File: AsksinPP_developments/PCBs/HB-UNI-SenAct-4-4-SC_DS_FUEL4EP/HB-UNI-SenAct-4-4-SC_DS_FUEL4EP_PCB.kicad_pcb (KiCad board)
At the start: 2 copper layers, 86 x 63 mm, 49 parts, among them J1 5V supply, J10 charge, J2 4x Push Buttons, J3 4x Relais, J4 5x LEDs, J5 ISP Programmer, J6 Accumulator, Q1 IRLU024N, Q2 BD238, Q4 IRF9Z34N, Q5 MCP1702-2802E_TO, SW1 SW_Push

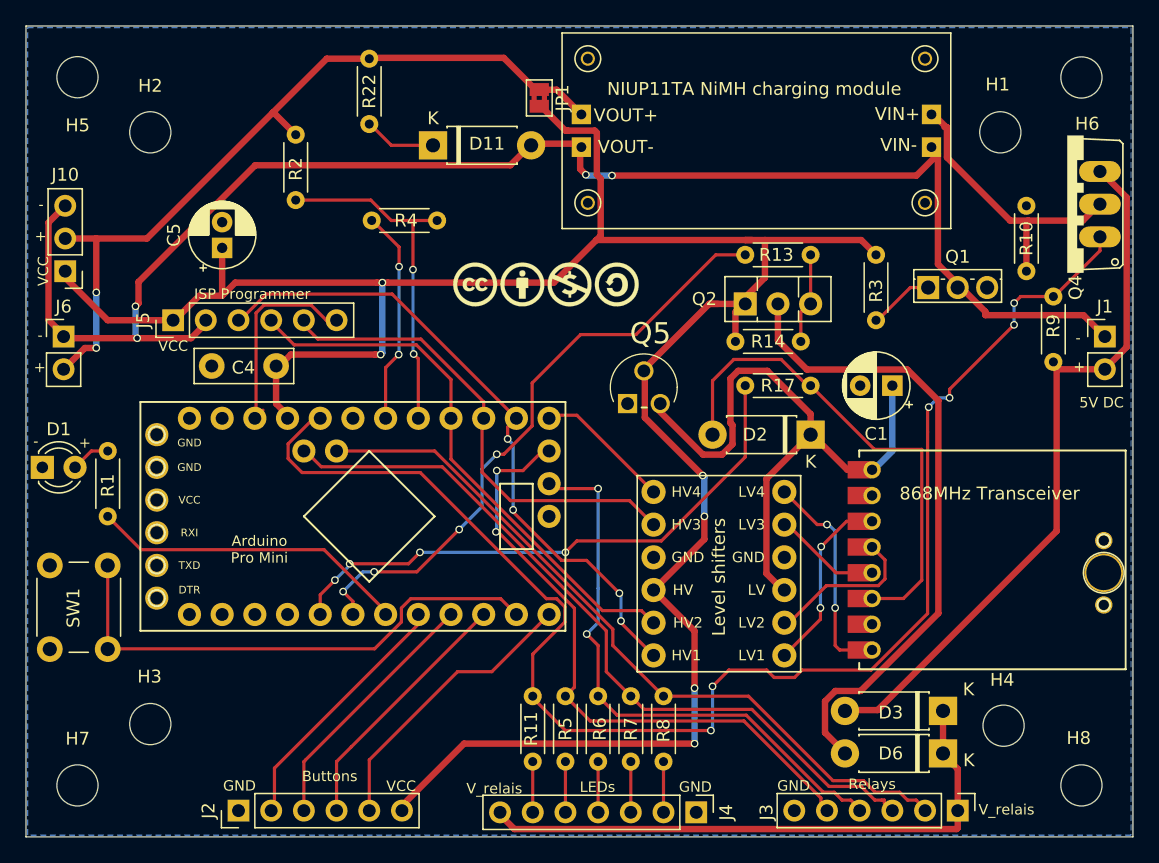
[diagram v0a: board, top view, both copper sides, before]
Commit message: PCBs/HB-UNI-SenAct-4-4-SC_DS_FUEL4EP: small fixes; HB-UNI-Sensor1-THPD-SHT85: Small flaw detected: SYSCLK calibration is missing; Please wait a bit for a fix
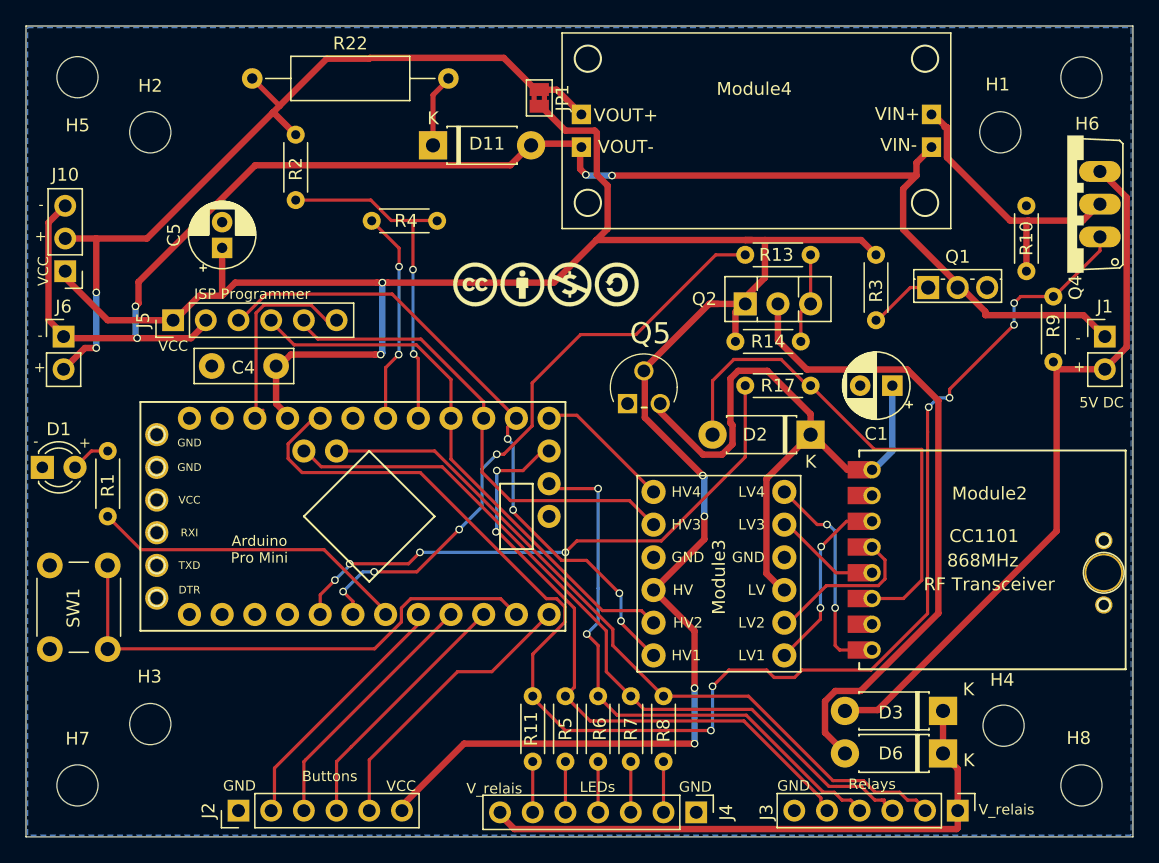
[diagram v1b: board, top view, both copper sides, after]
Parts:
- Module2: renamed from 868MHz Transceiver
- Module3: renamed from Level shifters; value Level Shifters -> 4_channel_LOGIC_LEVEL_CONVERTER
- Module4: renamed from NIUP11TA NiMH charging module
- R22: footprint Resistor_THT:R_Axial_DIN0204_L3.6mm_D1.6mm_P5.08mm_Horizontal -> Resistor_THT:R_Axial_DIN0309_L9.0mm_D3.2mm_P15.24mm_Horizontal
- moved R22 9.22 mm to (17.6, 4.08), turned to 0 degrees
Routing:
- net /plusBAT: track 62.3 -> 65.3 mm

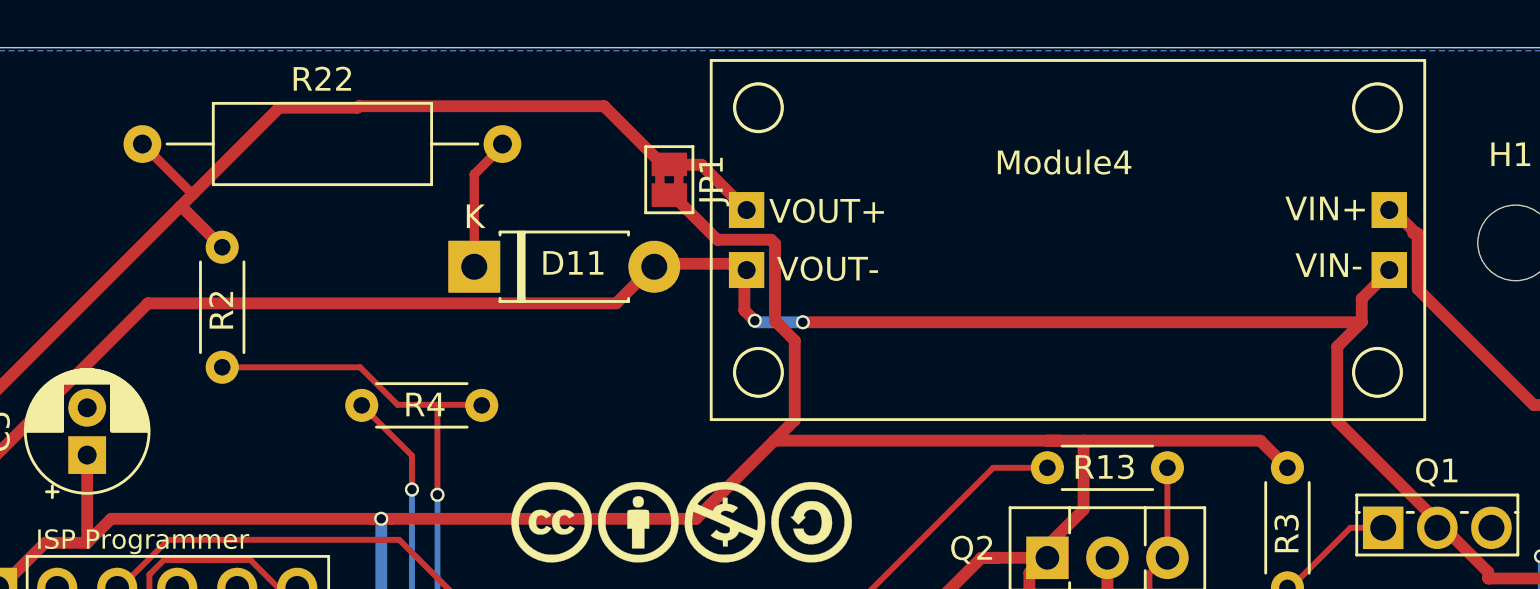
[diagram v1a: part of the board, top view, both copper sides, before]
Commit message: PCBs/HB-UNI-SenAct-4-4-SC_DS_FUEL4EP and PCBs/HM-LC-Bl1-FM_FUEL4EP: fixes of some geometry flaws that popped up during trial assembly
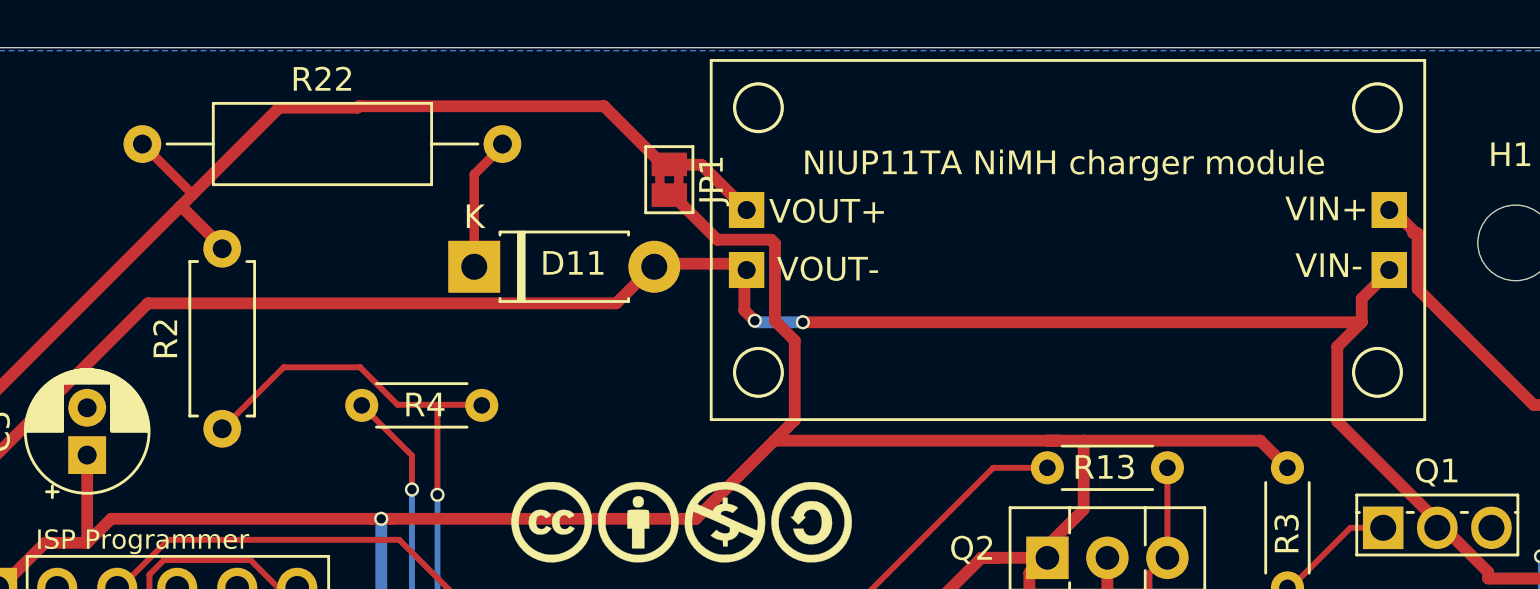
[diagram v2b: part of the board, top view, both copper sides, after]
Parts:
- NIUP11TA NiMH charger module: renamed from Module4
- R2: footprint Resistor_THT:R_Axial_DIN0204_L3.6mm_D1.6mm_P5.08mm_Horizontal -> Resistor_THT:R_Axial_DIN0207_L6.3mm_D2.5mm_P7.62mm_Horizontal
- moved R2 2.60 mm to (21.0, 16.1)
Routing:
- net /A0: track 27.1 -> 28.2 mm

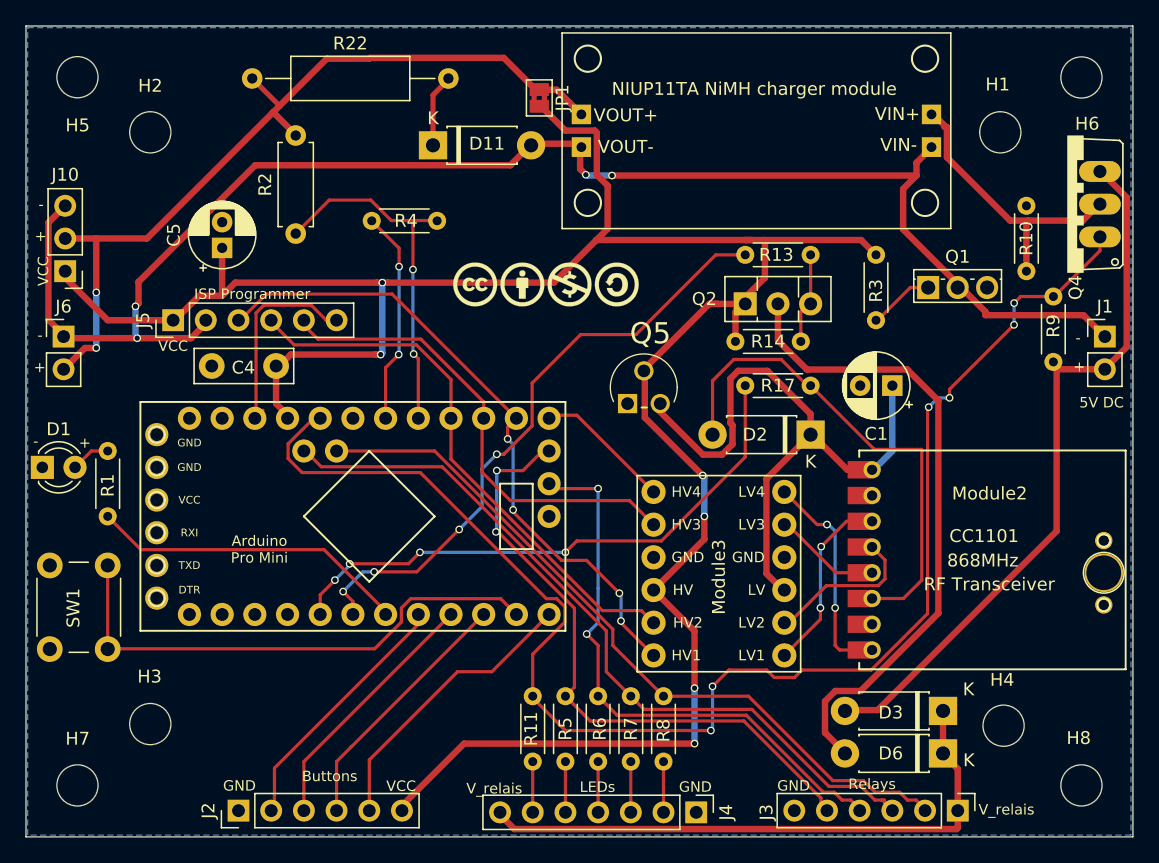
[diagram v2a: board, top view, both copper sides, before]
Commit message: PCBs/HM-LC-Bl1-FM_FUEL4EP and PCBs/HB-UNI-SenAct-4-4-SC_DS_FUEL4EP: fixes, new V1.2 PCB layouts
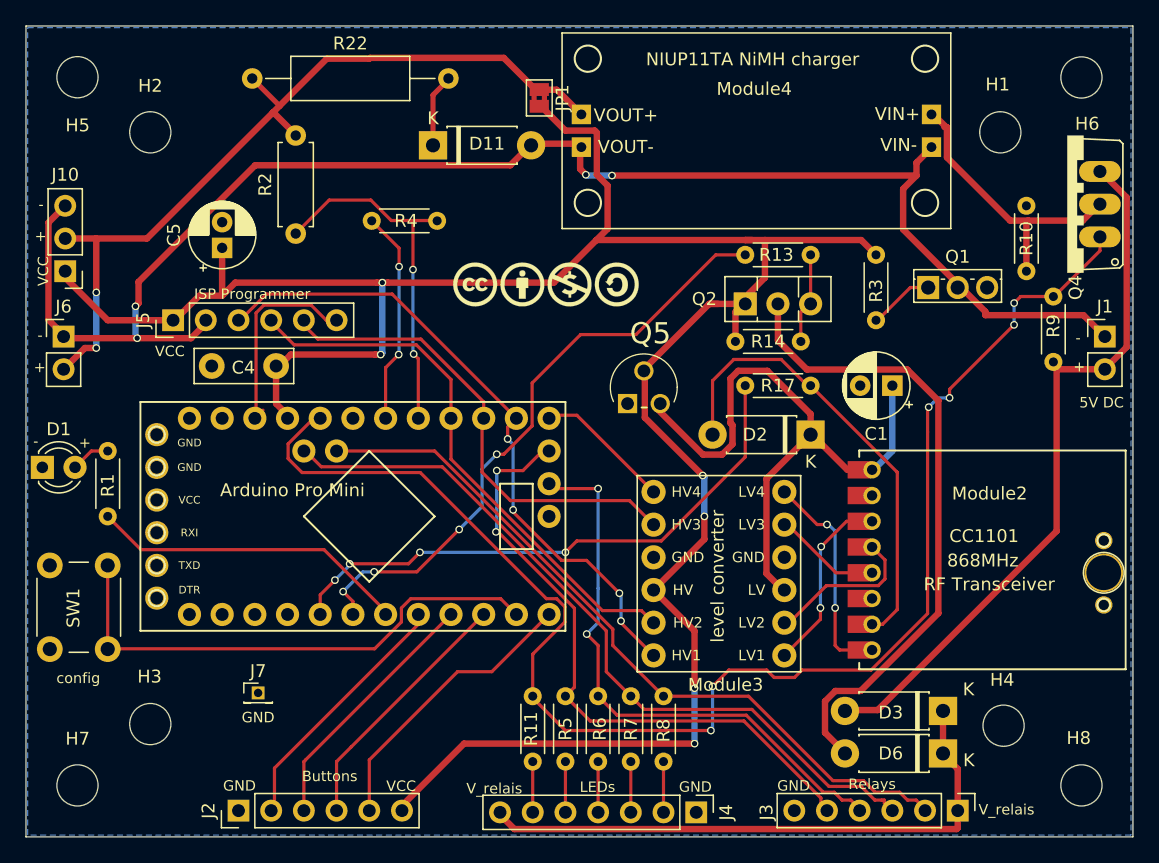
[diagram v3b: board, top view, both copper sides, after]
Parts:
- added J7: GND, Connector_PinHeader_1.27mm:PinHeader_1x01_P1.27mm_Vertical, F.Cu at (18.0, 51.8)
- Module3: value 4_channel_LOGIC_LEVEL_CONVERTER -> >VALUE
- Module4: renamed from NIUP11TA NiMH charger module
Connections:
- Module2 pad 6C: Net-(D2-Pad2) -> Net-(Module2-Pad6C)
- Module2 pad 7C: Net-(Module2-Pad7C) -> Net-(D2-Pad2)
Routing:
- net Net-(D2-Pad2): track 39.3 -> 37.3 mm
- net Net-(Module2-Pad7C): track 1.09 -> 0.00 mm
- net Net-(Module2-Pad6C): track 0.00 -> 1.06 mm
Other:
- board text added: "(C) FUEL4EP 11/2021 triple power switch for 230V demand switch zero standby power (only accumulators) V1.2"
- board text added: "config"
- board text removed: "(C) FUEL4EP 11/2021 triple power switch for 230V demand switch zero standby power (only accumulators)"
- board text removed: "Arduino Pro Mini"

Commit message: PCBs/HB-UNI-SenAct-4-4-SC_DS_FUEL4EP and PCBs/HM-LC-Bl1-FM_FUEL4EP: fix of R2 to 470kOhm
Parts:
- Module3: value >VALUE -> 4_channel_LOGIC_LEVEL_CONVERTER
- R2: value 200k -> 470k

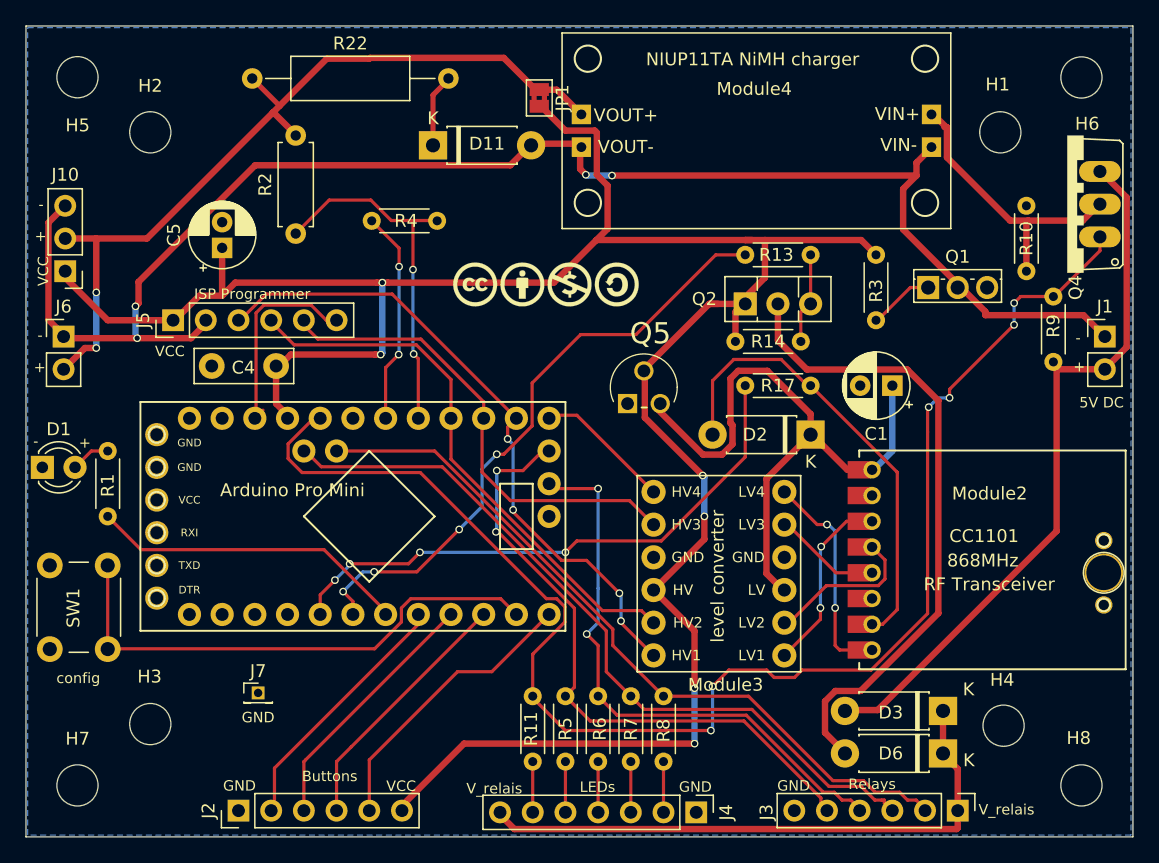
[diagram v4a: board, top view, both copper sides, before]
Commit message: major update: hb-ep-devices-addon V1.14; added sketches HB-UNI-Sensor1-AQ-BME680_KF_rLF and HB-UNI-SenAct-4-4-SC_DS; migration of all PPCBs to KiCAD 6
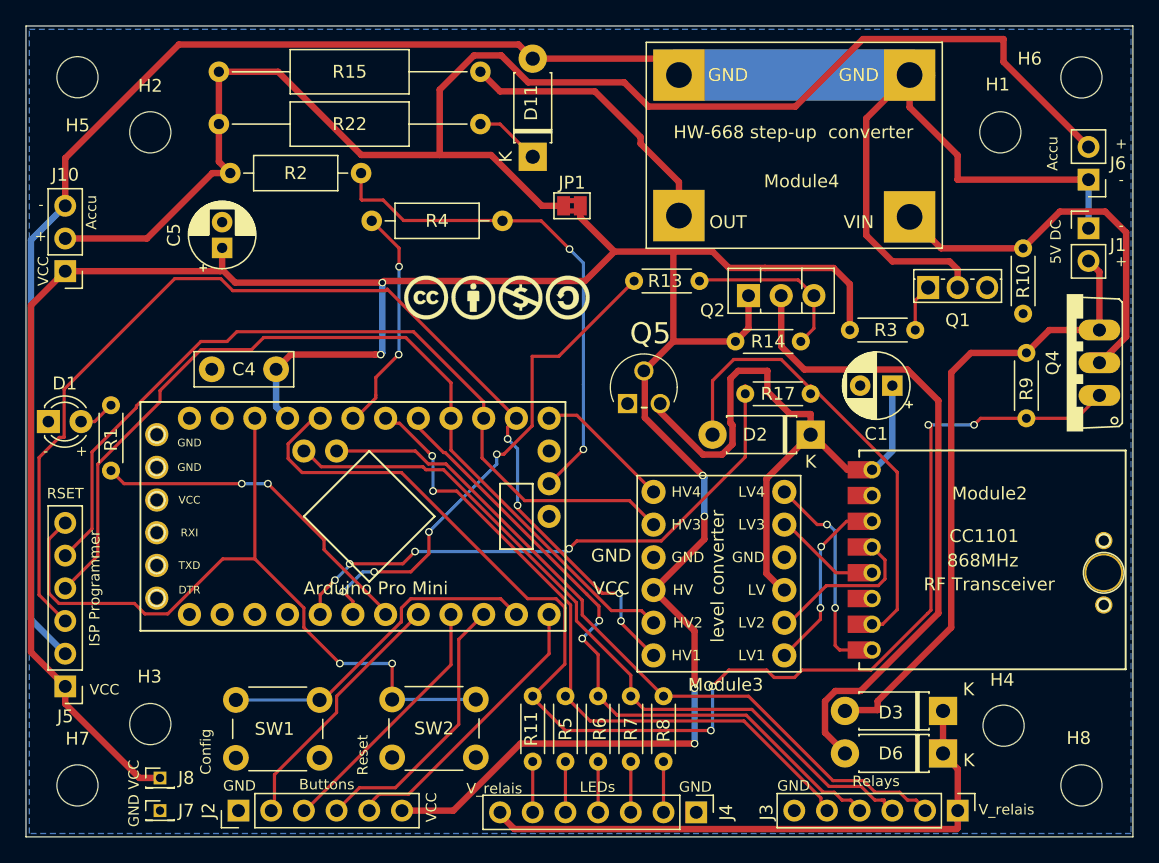
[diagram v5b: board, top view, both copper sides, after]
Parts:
- added J8: VCC, Connector_PinHeader_1.27mm:PinHeader_1x01_P1.27mm_Vertical, F.Cu at (10.4, 58.4)
- added R15: 22, Resistor_THT:R_Axial_DIN0309_L9.0mm_D3.2mm_P20.32mm_Horizontal, F.Cu at (15.0, 3.56)
- added SW2: SW_Push, Button_Switch_THT:SW_PUSH_6mm_H4.3mm, F.Cu at (28.4, 52.3)
- Module4: value NIUP11TA_NiMH_charger -> HW-668_step-up; footprint FUEL4EP:NIUP11TA_NiMH_charger -> FUEL4EP:HW-668_step-up
- R2: footprint Resistor_THT:R_Axial_DIN0207_L6.3mm_D2.5mm_P7.62mm_Horizontal -> Resistor_THT:R_Axial_DIN0207_L6.3mm_D2.5mm_P10.16mm_Horizontal
- R22: footprint Resistor_THT:R_Axial_DIN0309_L9.0mm_D3.2mm_P15.24mm_Horizontal -> Resistor_THT:R_Axial_DIN0309_L9.0mm_D3.2mm_P20.32mm_Horizontal
- R4: footprint Resistor_THT:R_Axial_DIN0204_L3.6mm_D1.6mm_P5.08mm_Horizontal -> Resistor_THT:R_Axial_DIN0207_L6.3mm_D2.5mm_P10.16mm_Horizontal
- moved J6 80.6 mm to (82.5, 11.9), turned to 180 degrees
- moved J5 29.7 mm to (3.05, 51.3), turned to 180 degrees
- moved SW1 22.6 mm to (22.8, 56.9), turned to 180 degrees
- moved Q4 12.3 mm to (80.9, 26.2)
- moved J7 11.9 mm to (10.4, 61.0)
- moved R13 8.87 mm to (52.3, 19.8)
- moved JP1 8.76 mm to (42.4, 14.0), turned to 0 degrees
- moved J1 8.51 mm to (82.5, 15.7)
- moved D11 7.80 mm to (39.4, 10.2), turned to 90 degrees
- moved R2 6.92 mm to (26.0, 11.4), turned to 180 degrees
- moved Module4 6.58 mm to (48.2, 1.27)
- moved R3 6.19 mm to (64.0, 23.6), turned to 0 degrees
- moved R22 4.39 mm to (15.0, 7.62)
- moved LOGO1 3.94 mm to (36.6, 21.1)
- moved D1 3.59 mm to (1.74, 30.7)
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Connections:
- J3 pad 4: /A6 -> /A0
- J3 pad 5: /A7 -> /A1
- Module1 pad 1A: Net-(Module1-Pad1A) -> unconnected-(Module1-Pad1A)
- Module1 pad 1C: Net-(Module1-Pad1C) -> unconnected-(Module1-Pad1C)
- Module1 pad 1D: Net-(Module1-Pad1D) -> unconnected-(Module1-Pad1D)
- Module1 pad 2C: Net-(Module1-Pad2C) -> unconnected-(Module1-Pad2C)
- Module1 pad 2D: Net-(Module1-Pad2D) -> unconnected-(Module1-Pad2D)
- Module1 pad 3B: /A7 -> unconnected-(Module1-Pad3B)
- Module1 pad 3C: Net-(Module1-Pad3C) -> unconnected-(Module1-Pad3C)
- Module1 pad 3D: Net-(Module1-Pad3D) -> unconnected-(Module1-Pad3D)
- Module1 pad 4C: Net-(Module1-Pad4C) -> unconnected-(Module1-Pad4C)
- Module1 pad 4D: Net-(Module1-Pad4D) -> unconnected-(Module1-Pad4D)
- Module1 pad 5D: Net-(Module1-Pad5D) -> unconnected-(Module1-Pad5D)
- Module1 pad 6A: Net-(Module1-Pad6A) -> /A2
- Module1 pad 6D: Net-(Module1-Pad6D) -> unconnected-(Module1-Pad6D)
- Module2 pad 2A: Net-(Module2-Pad2A) -> unconnected-(Module2-Pad2A)
- Module2 pad 6C: Net-(Module2-Pad6C) -> unconnected-(Module2-Pad6C)
- Module4 pad 1A: /V_CH -> /minusBAT
- Module4 pad 1C: /plusBAT -> /minusBAT
- Module4 pad 2A: /minusBAT -> /V_CH
- Module4 pad 2C: /minusBAT -> /Vcharge
- R2 pad 1: /A0 -> /A6
- R4 pad 1: /A1 -> /A2
- R4 pad 2: /A0 -> /A6
- R5 pad 1: /A7 -> /A1
- R6 pad 1: /A6 -> /A0
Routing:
- net /plusBAT: track 65.3 -> 119.7 mm, vias 2 -> 0
- net /A7: track 48.3 -> 0.00 mm, vias 2 -> 0
- net /RSET: track 15.5 -> 59.6 mm, vias 0 -> 2
- net /minusBAT: track 120.5 -> 158.0 mm, vias 4 -> 0
- net /MOSI: track 51.2 -> 87.3 mm
- net /A1: track 16.7 -> 52.7 mm
- net VCC: track 182.8 -> 214.8 mm
- net /MISO: track 37.2 -> 65.5 mm
- net /SCK: track 42.8 -> 70.5 mm
- net /A0: track 28.2 -> 52.6 mm
- net /Vcharge: track 0.00 -> 21.9 mm
- net /A2: track 0.00 -> 17.8 mm, vias 0 -> 2
- net /Config: track 41.1 -> 25.2 mm
- net /D3: track 47.8 -> 39.3 mm
- net /V_CH: track 22.4 -> 30.7 mm
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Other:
- net class Default removed
- net class battery removed
- net class power removed
- net class supply removed
- board text added: "(C) FUEL4EP 06/2023 triple power switch for 230V demand switch zero standby power (only accumulators) V1.3"
- board text added: "Accu"
- board text added: "Config"
- board text added: "RSET"
- board text added: "Reset"
- board text removed: "(C) FUEL4EP 11/2021 triple power switch for 230V demand switch zero standby power (only accumulators) V1.2"
- board text removed: "config"
